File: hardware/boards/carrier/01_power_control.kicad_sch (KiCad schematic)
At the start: 36 parts, among them J3 GND/CANL/CANH (TBD), Q1 IPB020N10N5LF, Q2 2N7002, Q3 2N7002, U3 LMX5069MS, U4 INA237AIDGSR, U5 TCAN3413DR

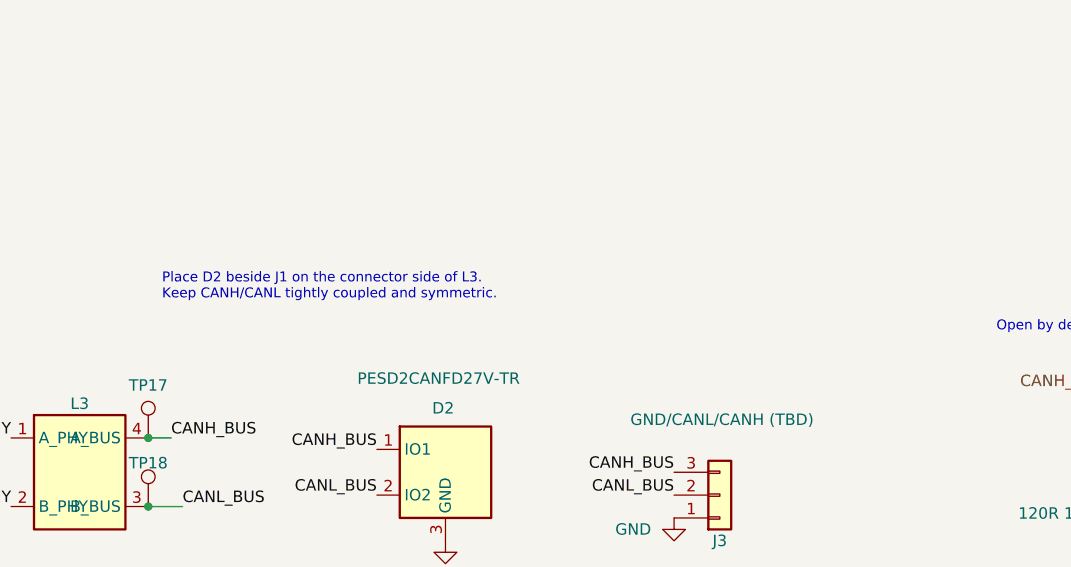
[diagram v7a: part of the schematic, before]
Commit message: Move carrier LED data to PA8
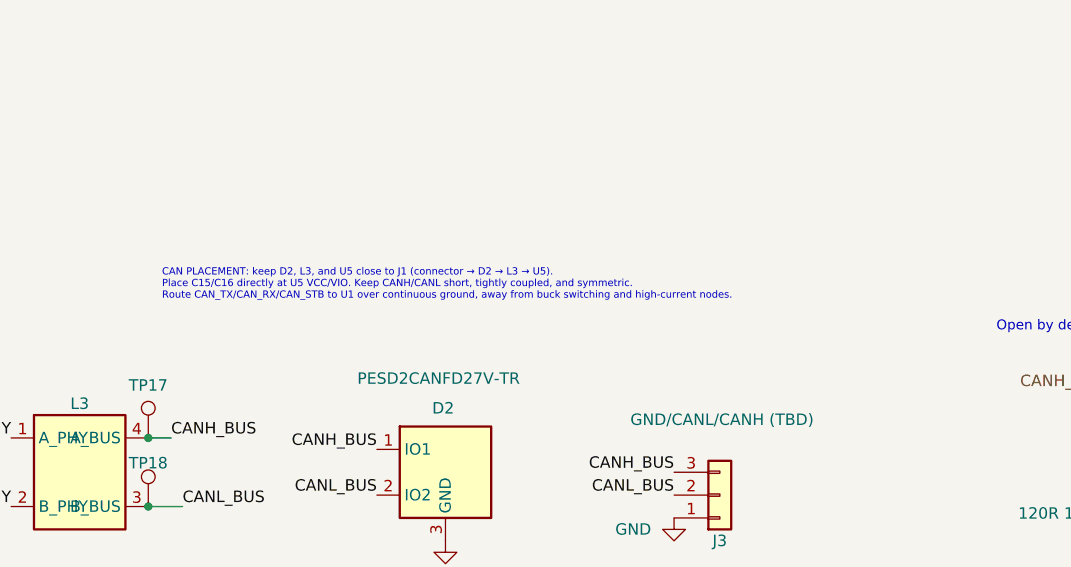
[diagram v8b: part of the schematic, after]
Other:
- note added: "CAN PLACEMENT: keep D2, L3, and U5 close to J1 (connector → D2 → L3 → U5). Place C15/C16 directly at U5 VCC/VIO. Keep CANH/CANL short, tightly coupled, and symmetric. Route CAN_TX/CAN_RX/CAN_STB to U1 over continuous ground, away from buck switching and high-current nodes."
- note removed: "Place D2 beside J1 on the connector side of L3. Keep CANH/CANL tightly coupled and symmetric."
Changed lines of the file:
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@@
 		)
 	)
-	(text "Place D2 beside J1 on the connector side of L3.\nKeep CANH/CANL tightly coupled and symmetric."
+	(text "CAN PLACEMENT: keep D2, L3, and U5 close to J1 (connector → D2 → L3 → U5).\nPlace C15/C16 directly at U5 VCC/VIO. Keep CANH/CANL short, tightly coupled, and symmetric.\nRoute CAN_TX/CAN_RX/CAN_STB to U1 over continuous ground, away from buck switching and high-current nodes."
 		(exclude_from_sim no)
 		(at 132.334 233.68 0)
 		(effects
 			(font
-				(size 1.1 1.1)
+				(size 0.8 0.8)
 			)
 			(justify left bottom)
@@
 		)
 	)
-	(hierarchical_label "CANL_BUS"
-		(shape bidirectional)
-		(at 238.76 265.43 180)
-		(effects
-			(font
-				(size 1.27 1.27)
-			)
-			(justify right bottom)
-		)
-	)
 	(label "INA_INM_FILT"
 		(at 228.6 134.62 180)
@@
 	(label "CANH_BUS"
 		(at 156.21 250.19 180)
-		(effects
-			(font
-				(size 1.27 1.27)
-			)
-			(justify right bottom)
-		)
-	)
-	(hierarchical_label "CANH_BUS"
-		(shape bidirectional)
-		(at 238.76 242.57 180)
 		(effects
 			(font
@@
 		)
 	)
+	(hierarchical_label "CANL_BUS"
+		(shape bidirectional)
+		(at 238.76 265.43 180)
+		(effects
+			(font
+				(size 1.27 1.27)
+			)
+			(justify right bottom)
+		)
+	)
 	(hierarchical_label "PD_IRQ"
 		(shape output)
@@
 		)
 	)
+	(hierarchical_label "CANH_BUS"
+		(shape bidirectional)
+		(at 238.76 242.57 180)
+		(effects
+			(font
+				(size 1.27 1.27)
+			)
+			(justify right bottom)
+		)
+	)
